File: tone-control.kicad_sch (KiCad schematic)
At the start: 38 parts, among them U2501 TL074

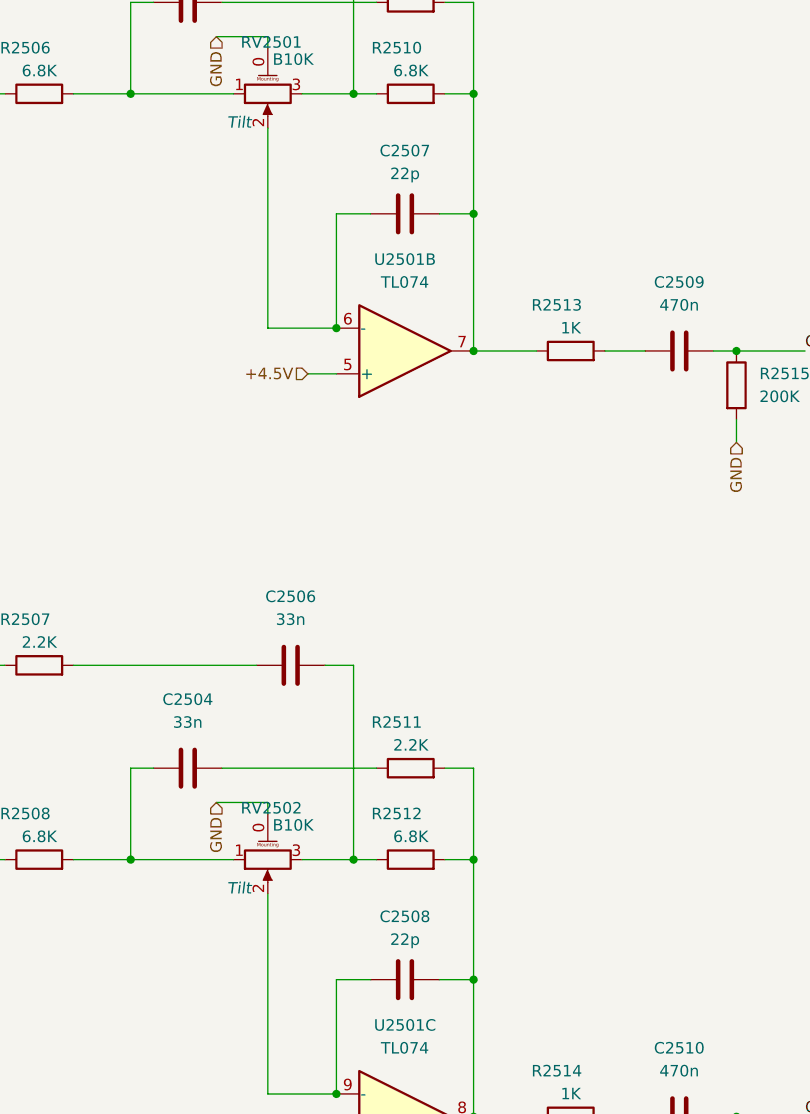
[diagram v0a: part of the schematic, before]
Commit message: Add JLC parts numbers
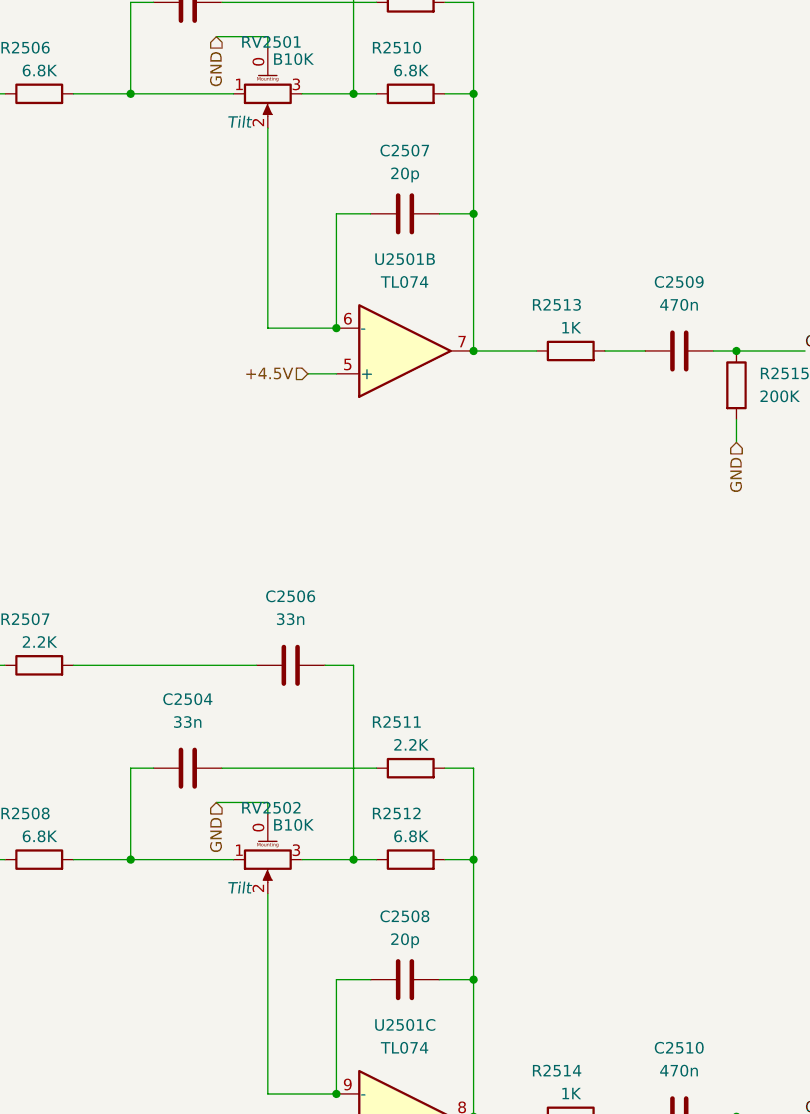
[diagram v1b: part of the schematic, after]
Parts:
- C2501, C2502, C2509, C2510: LCSC (none) -> C651004; Role (none) -> audio-coupling
- C2503, C2504, C2505, C2506: LCSC (none) -> C106856; Role (none) -> audio-filter
- C2507, C2508: value 22p -> 20p; LCSC (none) -> C105621; Role (none) -> audio-filter
- C2511: LCSC (none) -> C497032; Role (none) -> ic-bypass
- D2501, D2502, D2503, D2504: LCSC (none) -> C20936
- R2501, R2502: LCSC (none) -> C234360
- R2503, R2504, R2515, R2516: LCSC (none) -> C203392
- R2505, R2507, R2509, R2511: LCSC (none) -> C328351
- R2506, R2508, R2510, R2512: LCSC (none) -> C328374
- R2513, R2514: LCSC (none) -> C2907002
- U2501: LCSC (none) -> C6963
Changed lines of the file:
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@@
+      (effects (font (size 1.27 1.27)) hide)
+    )
+    (property "LCSC" "C328351" (id 4) (at 127.635 36.83 0)
       (effects (font (size 1.27 1.27)) hide)
     )
@@
     )
     (property "Datasheet" "http://www.ti.com/lit/ds/symlink/tl071.pdf" (id 3) (at 128.27 80.645 0)
+      (effects (font (size 1.27 1.27)) hide)
+    )
+    (property "LCSC" "C6963" (id 4) (at 127 75.565 0)
       (effects (font (size 1.27 1.27)) hide)
     )
@@
       (effects (font (size 1.27 1.27)) hide)
     )
+    (property "LCSC" "C2907002" (id 4) (at 145.415 160.655 0)
+      (effects (font (size 1.27 1.27)) hide)
+    )
     (pin "1")
     (pin "2")
@@
       (effects (font (size 1.27 1.27)) hide)
     )
+    (property "LCSC" "C328374" (id 4) (at 127.635 46.99 0)
+      (effects (font (size 1.27 1.27)) hide)
+    )
     (pin "1")
     (pin "2")
@@
       (effects (font (size 1.27 1.27)) hide)
     )
+    (property "LCSC" "C328374" (id 4) (at 86.36 132.08 0)
+      (effects (font (size 1.27 1.27)) hide)
+    )
     (pin "1")
     (pin "2")
@@
       (effects (font (size 1.27 1.27)) hide)
     )
+    (property "LCSC" "C203392" (id 4) (at 48.26 138.43 0)
+      (effects (font (size 1.27 1.27)) hide)
+    )
     (pin "1")
     (pin "2")
@@
     )
     (property "Datasheet" "~" (id 3) (at 27.94 138.43 0)
+      (effects (font (size 1.27 1.27)) hide)
+    )
+    (property "LCSC" "C234360" (id 4) (at 27.94 138.43 0)
       (effects (font (size 1.27 1.27)) hide)
     )
@@
     )
     (property "Datasheet" "~" (id 3) (at 127.635 121.92 0)
+      (effects (font (size 1.27 1.27)) hide)
+    )
+    (property "LCSC" "C328351" (id 4) (at 127.635 121.92 0)
       (effects (font (size 1.27 1.27)) hide)
     )
@@
       (effects (font (size 1.27 1.27)) hide)
     )
+    (property "LCSC" "C651004" (id 4) (at 38.1 49.53 0)
+      (effects (font (size 1.27 1.27)) hide)
+    )
+    (property "Role" "audio-coupling" (id 5) (at 38.1 49.53 0)
+      (effects (font (size 1.27 1.27)) hide)
+    )
     (pin "1")
     (pin "2")
@@
       (effects (font (size 1.27 1.27)) hide)
     )
+    (property "LCSC" "C328351" (id 4) (at 86.36 110.49 0)
+      (effects (font (size 1.27 1.27)) hide)
+    )
     (pin "1")
     (pin "2")
@@
     (in_bom yes) (on_board yes) (fields_autoplaced)
     (property "Reference" "C2507" (id 0) (at 127 53.34 90))
-    (property "Value" "22p" (id 1) (at 127 55.88 90))
+    (property "Value" "20p" (id 1) (at 127 55.88 90))
     (property "Footprint" "Capacitor_SMD:C_0603_1608Metric_Pad1.08x0.95mm_HandSolder" (id 2) (at 130.81 59.3598 0)
       (effects (font (size 1.27 1.27)) hide)
     )
     (property "Datasheet" "~" (id 3) (at 127 60.325 0)
+      (effects (font (size 1.27 1.27)) hide)
+    )
+    (property "LCSC" "C105621" (id 4) (at 127 60.325 0)
+      (effects (font (size 1.27 1.27)) hide)
+    )
+    (property "Role" "audio-filter" (id 5) (at 127 60.325 0)
       (effects (font (size 1.27 1.27)) hide)
     )
@@
     )
     (property "Datasheet" "http://www.ti.com/lit/ds/symlink/tl071.pdf" (id 3) (at 63.5 137.16 0)
+      (effects (font (size 1.27 1.27)) hide)
+    )
+    (property "LCSC" "C6963" (id 4) (at 62.23 132.08 0)
       (effects (font (size 1.27 1.27)) hide)
     )
@@
       (effects (font (size 1.27 1.27)) hide)
     )
+    (property "LCSC" "C203392" (id 4) (at 48.26 53.34 0)
+      (effects (font (size 1.27 1.27)) hide)
+    )
     (pin "1")
     (pin "2")
@@
       (effects (font (size 1.27 1.27)) hide)
     )
+    (property "LCSC" "C651004" (id 4) (at 157.48 75.565 0)
+      (effects (font (size 1.27 1.27)) hide)
+    )
+    (property "Role" "audio-coupling" (id 5) (at 157.48 75.565 0)
+      (effects (font (size 1.27 1.27)) hide)
+    )
     (pin "1")
     (pin "2")
@@
       (effects (font (size 1.27 1.27)) hide)
     )
+    (property "LCSC" "C106856" (id 4) (at 102.87 121.92 0)
+      (effects (font (size 1.27 1.27)) hide)
+    )
+    (property "Role" "audio-filter" (id 5) (at 102.87 121.92 0)
+      (effects (font (size 1.27 1.27)) hide)
+    )
     (pin "1")
     (pin "2")
@@
     )
     (property "Datasheet" "http://www.ti.com/lit/ds/symlink/tl071.pdf" (id 3) (at 278.13 29.21 0)
+      (effects (font (size 1.27 1.27)) hide)
+    )
+    (property "LCSC" "C6963" (id 4) (at 276.86 34.29 0)
       (effects (font (size 1.27 1.27)) hide)
     )
@@
       (effects (font (size 1.27 1.27)) hide)
     )
+    (property "LCSC" "C328374" (id 4) (at 127.635 132.08 0)
+      (effects (font (size 1.27 1.27)) hide)
+    )
     (pin "1")
     (pin "2")
@@
     )
     (property "Datasheet" "http://www.ti.com/lit/ds/symlink/tl071.pdf" (id 3) (at 63.5 52.07 0)
+      (effects (font (size 1.27 1.27)) hide)
+    )
+    (property "LCSC" "C6963" (id 4) (at 62.23 46.99 0)
       (effects (font (size 1.27 1.27)) hide)
     )
@@
       (effects (font (size 1.27 1.27)) hide)
     )
+    (property "LCSC" "C234360" (id 4) (at 27.94 53.34 0)
+      (effects (font (size 1.27 1.27)) hide)
+    )
     (pin "1")
     (pin "2")
@@
       (effects (font (size 1.27 1.27)) hide)
     )
+    (property "LCSC" "C203392" (id 4) (at 163.83 164.465 0)
+      (effects (font (size 1.27 1.27)) hide)
+    )
     (pin "1")
     (pin "2")
@@
     )
     (property "Datasheet" "~" (id 3) (at 232.41 121.92 0)
+      (effects (font (size 1.27 1.27)) hide)
+    )
+    (property "LCSC" "C20936" (id 4) (at 232.41 121.92 0)
       (effects (font (size 1.27 1.27)) hide)
     )
@@
       (effects (font (size 1.27 1.27)) hide)
     )
+    (property "LCSC" "C106856" (id 4) (at 114.3 110.49 0)
+      (effects (font (size 1.27 1.27)) hide)
+    )
+    (property "Role" "audio-filter" (id 5) (at 114.3 110.49 0)
+      (effects (font (size 1.27 1.27)) hide)
+    )
     (pin "1")
     (pin "2")
@@
       (effects (font (size 1.27 1.27)) hide)
     )
+    (property "LCSC" "C497032" (id 4) (at 262.89 34.29 0)
+      (effects (font (size 1.27 1.27)) hide)
+    )
+    (property "Role" "ic-bypass" (id 5) (at 262.89 34.29 0)
+      (effects (font (size 1.27 1.27)) hide)
+    )
     (pin "1")
     (pin "2")
@@
     (in_bom yes) (on_board yes) (fields_autoplaced)
     (property "Reference" "C2508" (id 0) (at 127 138.43 90))
-    (property "Value" "22p" (id 1) (at 127 140.97 90))
+    (property "Value" "20p" (id 1) (at 127 140.97 90))
     (property "Footprint" "Capacitor_SMD:C_0603_1608Metric_Pad1.08x0.95mm_HandSolder" (id 2) (at 130.81 144.4498 0)
       (effects (font (size 1.27 1.27)) hide)
@@
       (effects (font (size 1.27 1.27)) hide)
     )
+    (property "LCSC" "C105621" (id 4) (at 127 145.415 0)
+      (effects (font (size 1.27 1.27)) hide)
+    )
+    (property "Role" "audio-filter" (id 5) (at 127 145.415 0)
+      (effects (font (size 1.27 1.27)) hide)
+    )
     (pin "1")
     (pin "2")
@@
     )
     (property "Datasheet" "~" (id 3) (at 163.83 79.375 0)
+      (effects (font (size 1.27 1.27)) hide)
+    )
+    (property "LCSC" "C203392" (id 4) (at 163.83 79.375 0)
       (effects (font (size 1.27 1.27)) hide)
     )
@@
       (effects (font (size 1.27 1.27)) hide)
     )
+    (property "LCSC" "C328351" (id 4) (at 86.36 25.4 0)
+      (effects (font (size 1.27 1.27)) hide)
+    )
     (pin "1")
     (pin "2")
@@
       (effects (font (size 1.27 1.27)) hide)
     )
+    (property "LCSC" "C2907002" (id 4) (at 145.415 75.565 0)
+      (effects (font (size 1.27 1.27)) hide)
+    )
     (pin "1")
     (pin "2")
@@
     )
     (property "Datasheet" "~" (id 3) (at 198.12 39.37 0)
+      (effects (font (size 1.27 1.27)) hide)
+    )
+    (property "LCSC" "C20936" (id 4) (at 198.12 39.37 0)
       (effects (font (size 1.27 1.27)) hide)
     )
@@
       (effects (font (size 1.27 1.27)) hide)
     )
+    (property "LCSC" "C651004" (id 4) (at 38.1 134.62 0)
+      (effects (font (size 1.27 1.27)) hide)
+    )
+    (property "Role" "audio-coupling" (id 5) (at 38.1 134.62 0)
+      (effects (font (size 1.27 1.27)) hide)
+    )
     (pin "1")
     (pin "2")
@@
       (effects (font (size 1.27 1.27)) hide)
     )
+    (property "LCSC" "C106856" (id 4) (at 102.87 36.83 0)
+      (effects (font (size 1.27 1.27)) hide)
+    )
+    (property "Role" "audio-filter" (id 5) (at 102.87 36.83 0)
+      (effects (font (size 1.27 1.27)) hide)
+    )
     (pin "1")
     (pin "2")
@@
       (effects (font (size 1.27 1.27)) hide)
     )
+    (property "LCSC" "C651004" (id 4) (at 157.48 160.655 0)
+      (effects (font (size 1.27 1.27)) hide)
+    )
+    (property "Role" "audio-coupling" (id 5) (at 157.48 160.655 0)
+      (effects (font (size 1.27 1.27)) hide)
+    )
     (pin "1")
     (pin "2")
@@
     )
     (property "Datasheet" "~" (id 3) (at 198.12 121.92 0)
+      (effects (font (size 1.27 1.27)) hide)
+    )
+    (property "LCSC" "C20936" (id 4) (at 198.12 121.92 0)
       (effects (font (size 1.27 1.27)) hide)
     )
@@
       (effects (font (size 1.27 1.27)) hide)
     )
+    (property "LCSC" "C328374" (id 4) (at 86.36 46.99 0)
+      (effects (font (size 1.27 1.27)) hide)
+    )
     (pin "1")
     (pin "2")
@@
     )
     (property "Datasheet" "~" (id 3) (at 232.41 39.37 0)
+      (effects (font (size 1.27 1.27)) hide)
+    )
+    (property "LCSC" "C20936" (id 4) (at 232.41 39.37 0)
       (effects (font (size 1.27 1.27)) hide)
     )
@@
       (effects (font (size 1.27 1.27)) hide)
     )
+    (property "LCSC" "C106856" (id 4) (at 114.3 25.4 0)
+      (effects (font (size 1.27 1.27)) hide)
+    )
+    (property "Role" "audio-filter" (id 5) (at 114.3 25.4 0)
+      (effects (font (size 1.27 1.27)) hide)
+    )
     (pin "1")
     (pin "2")
@@
       (effects (font (size 1.27 1.27)) hide)
     )
+    (property "LCSC" "C6963" (id 4) (at 127 160.655 0)
+      (effects (font (size 1.27 1.27)) hide)
+    )
